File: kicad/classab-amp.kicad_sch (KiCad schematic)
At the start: 65 parts, among them J1 SPEAKER, J3 INPUT, Q1 BC547, Q10 MJL3218C, Q11 BD140, Q12 MJL1302C, Q13 BC547, Q14 BC557, Q2 BC547, Q3 BC557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

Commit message: Adjustments
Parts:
- removed D10, D7, D8, D9: 1N5400, Diode_THT:D_DO-201AD_P15.24mm_Horizontal, symbol Diode:1N5400
- removed D3, D6: 1N4001, Diode_THT:D_DO-41_SOD81_P10.16mm_Horizontal, symbol Diode:1N4001
- added D10, D3, D6, D7, D8, D9: 1N4004, Diode_THT:D_DO-41_SOD81_P10.16mm_Horizontal, symbol Diode:1N4004
- C4: footprint Capacitor_THT:CP_Radial_D4.0mm_P1.50mm -> Capacitor_THT:CP_Radial_D8.0mm_P5.00mm
- C6: footprint (none) -> Capacitor_THT:C_Rect_L7.2mm_W3.0mm_P5.00mm_FKS2_FKP2_MKS2_MKP2
- R13, R6: value 47k -> 10k
- R5: value 2.2k -> 1k
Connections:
- net B+: now also D7.1 (K), D8.1 (K)
- net B-: now also D10.2 (A), D9.2 (A)
- net GND: now also D10.1 (K), D7.2 (A)
- net at Q10.3 (E), R16.1, R18.2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: now also D8.2 (A)
- net at C5.2, C6.1, Q6.2 (C)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: now also D6.2 (A)
- net at C12.1, Q14.1 (C): now also D3.2 (A)
- net at Q12.3 (E), R17.2, R19.1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: now also D9.1 (K)
- net at C11.1, Q13.1 (C): now also D6.1 (K)
- net at C6.2, Q11.3 (B), Q7.1 (E)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: now also D3.1 (K)
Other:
- moved on the sheet: R6

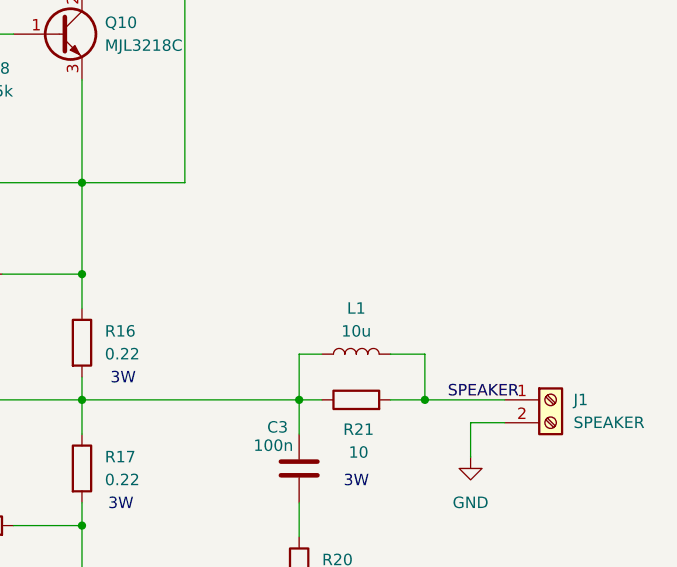
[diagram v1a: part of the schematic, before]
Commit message: Added Zobel image
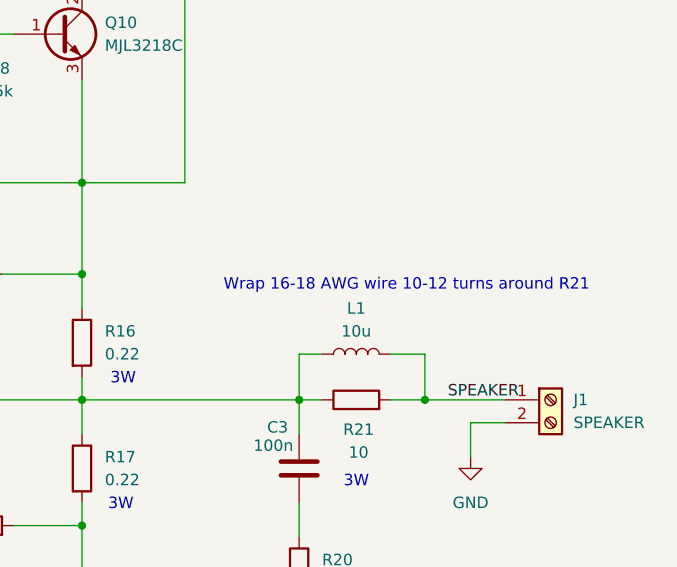
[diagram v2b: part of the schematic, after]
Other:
- note added: "Wrap 16-18 AWG wire 10-12 turns around R21"
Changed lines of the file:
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@@
+		)
+	)
+	(text "Wrap 16-18 AWG wire 10-12 turns around R21"
+		(exclude_from_sim no)
+		(at 257.048 74.93 0)
+		(effects
+			(font
+				(size 1.27 1.27)
+			)
 		)
 	)

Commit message: Added ver 2 SPICE design
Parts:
- added C7: 10n, Capacitor_THT:C_Rect_L7.2mm_W3.0mm_P5.00mm_FKS2_FKP2_MKS2_MKP2, symbol Device:C
- R15: value 10 -> 220
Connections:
- net CHASSIS: now also C7.2
- net GND: now also C7.1
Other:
- moved on the sheet: D8, R15
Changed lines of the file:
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@@
 	)
 	(junction
-		(at 64.77 115.57)
+		(at 53.34 118.11)
 		(diameter 0)
 		(color 0 0 0 0)
@@
 	(wire
 		(pts
+			(xy 64.77 102.87) (xy 64.77 106.68)
+		)
+		(stroke
+			(width 0)
+			(type default)
+		)
+	)
+	(wire
+		(pts
 			(xy 168.91 107.95) (xy 168.91 118.11)
 		)
@@
 	(wire
 		(pts
-			(xy 232.41 29.21) (xy 232.41 34.29)
+			(xy 232.41 29.21) (xy 232.41 35.56)
 		)
 		(stroke
@@
 	(wire
 		(pts
-			(xy 64.77 115.57) (xy 64.77 116.84)
+			(xy 53.34 118.11) (xy 53.34 119.38)
 		)
 		(stroke
@@
 	(wire
 		(pts
-			(xy 182.88 134.62) (xy 189.23 134.62)
+			(xy 180.34 134.62) (xy 189.23 134.62)
 		)
 		(stroke
@@
 	(wire
 		(pts
-			(xy 176.53 118.11) (xy 182.88 118.11)
+			(xy 176.53 118.11) (xy 180.34 118.11)
 		)
 		(stroke
@@
 	(wire
 		(pts
-			(xy 182.88 118.11) (xy 182.88 134.62)
+			(xy 180.34 118.11) (xy 180.34 134.62)
 		)
 		(stroke
@@
 	(wire
 		(pts
-			(xy 64.77 114.3) (xy 64.77 115.57)
+			(xy 53.34 114.3) (xy 53.34 118.11)
 		)
 		(stroke
@@
 	(wire
 		(pts
+			(xy 53.34 118.11) (xy 64.77 118.11)
+		)
+		(stroke
+			(width 0)
+			(type default)
+		)
+	)
+	(wire
+		(pts
 			(xy 180.34 68.58) (xy 180.34 38.1)
 		)
@@
 	(wire
 		(pts
+			(xy 53.34 102.87) (xy 64.77 102.87)
+		)
+		(stroke
+			(width 0)
+			(type default)
+		)
+	)
+	(wire
+		(pts
 			(xy 168.91 128.27) (xy 168.91 130.81)
 		)
@@
 	(wire
 		(pts
+			(xy 64.77 114.3) (xy 64.77 118.11)
+		)
+		(stroke
+			(width 0)
+			(type default)
+		)
+	)
+	(wire
+		(pts
 			(xy 46.99 95.25) (xy 46.99 96.52)
 		)
@@
 	(wire
 		(pts
-			(xy 64.77 106.68) (xy 64.77 102.87)
+			(xy 53.34 106.68) (xy 53.34 102.87)
 		)
 		(stroke
@@
 	(wire
 		(pts
-			(xy 232.41 41.91) (xy 232.41 63.5)
+			(xy 232.41 43.18) (xy 232.41 63.5)
 		)
 		(stroke
@@
 	(text "3W"
 		(exclude_from_sim no)
-		(at 68.072 115.57 0)
+		(at 56.896 114.3 0)
 		(effects
 			(font
@@
 	(symbol
 		(lib_id "Diode:1N4004")
-		(at 232.41 38.1 270)
+		(at 232.41 39.37 270)
 		(unit 1)
 		(exclude_from_sim no)
@@
 		(fields_autoplaced yes)
 		(property "Reference" "D8"
-			(at 234.95 36.8299 90)
+			(at 234.95 38.0999 90)
 			(effects
 				(font
@@
 		)
 		(property "Value" "1N4004"
-			(at 234.95 39.3699 90)
+			(at 234.95 40.6399 90)
 			(effects
 				(font
@@
 		)
 		(property "Footprint" "Diode_THT:D_DO-41_SOD81_P10.16mm_Horizontal"
-			(at 227.965 38.1 0)
+			(at 227.965 39.37 0)
 			(effects
 				(font
@@
 		)
 		(property "Datasheet" "http://www.vishay.com/docs/88503/1n4001.pdf"
-			(at 232.41 38.1 0)
+			(at 232.41 39.37 0)
 			(effects
 				(font
@@
 		)
 		(property "Description" "400V 1A General Purpose Rectifier Diode, DO-41"
-			(at 232.41 38.1 0)
+			(at 232.41 39.37 0)
 			(effects
 				(font
@@
 		)
 		(property "Sim.Device" "D"
-			(at 232.41 38.1 0)
+			(at 232.41 39.37 0)
 			(effects
 				(font
@@
 		)
 		(property "Sim.Pins" "1=K 2=A"
-			(at 232.41 38.1 0)
+			(at 232.41 39.37 0)
 			(effects
 				(font
@@
 	(symbol
 		(lib_id "Device:R")
-		(at 64.77 110.49 180)
+		(at 53.34 110.49 180)
 		(unit 1)
 		(exclude_from_sim no)
@@
 		(fields_autoplaced yes)
 		(property "Reference" "R15"
-			(at 67.31 109.2199 0)
+			(at 55.88 109.2199 0)
 			(effects
 				(font
@@
 			)
 		)
-		(property "Value" "10"
-			(at 67.31 111.7599 0)
+		(property "Value" "220"
+			(at 55.88 111.7599 0)
 			(effects
 				(font
@@
 		)
 		(property "Footprint" "Resistor_THT:R_Axial_DIN0414_L11.9mm_D4.5mm_P15.24mm_Horizontal"
-			(at 66.548 110.49 90)
+			(at 55.118 110.49 90)
 			(effects
 				(font
@@
 		)
 		(property "Datasheet" "~"
-			(at 64.77 110.49 0)
+			(at 53.34 110.49 0)
 			(effects
 				(font
@@
 		)
 		(property "Description" "Resistor"
-			(at 64.77 110.49 0)
+			(at 53.34 110.49 0)
 			(effects
 				(font
@@
 	(symbol
 		(lib_id "power:PWR_FLAG")
-		(at 64.77 115.57 90)
+		(at 53.34 118.11 90)
 		(unit 1)
 		(exclude_from_sim no)
@@
 		(fields_autoplaced yes)
 		(property "Reference" "#FLG01"
-			(at 62.865 115.57 0)
+			(at 51.435 118.11 0)
 			(effects
 				(font
@@
 		)
 		(property "Value" "PWR_FLAG"
-			(at 60.96 115.5699 90)
+			(at 49.53 118.1099 90)
 			(effects
 				(font
@@
 		)
 		(property "Footprint" ""
-			(at 64.77 115.57 0)
+			(at 53.34 118.11 0)
 			(effects
 				(font
@@
 		)
 		(property "Datasheet" "~"
-			(at 64.77 115.57 0)
+			(at 53.34 118.11 0)
 			(effects
 				(font
@@
 		)
 		(property "Description" "Special symbol for telling ERC where power comes from"
-			(at 64.77 115.57 0)
+			(at 53.34 118.11 0)
 			(effects
 				(font
@@
 	(symbol
 		(lib_id "power:GNDPWR")
-		(at 64.77 116.84 0)
+		(at 53.34 119.38 0)
 		(unit 1)
 		(exclude_from_sim no)
@@
 		(fields_autoplaced yes)
 		(property "Reference" "#PWR011"
-			(at 64.77 121.92 0)
+			(at 53.34 124.46 0)
 			(effects
 				(font
@@
 		)
 		(property "Value" "CHASSIS"
-			(at 64.643 120.65 0)
+			(at 53.213 123.19 0)
 			(effects
 				(font
@@
 		)
 		(property "Footprint" ""
-			(at 64.77 118.11 0)
+			(at 53.34 120.65 0)
 			(effects
 				(font
@@
 		)
 		(property "Datasheet" ""
-			(at 64.77 118.11 0)
+			(at 53.34 120.65 0)
 			(effects
 				(font
@@
 		)
 		(property "Description" "Power symbol creates a global label with name \"GNDPWR\" , global ground"
-			(at 64.77 116.84 0)
+			(at 53.34 119.38 0)
 			(effects
 				(font
@@
 					(unit 1)
 				)
+			)
+		)
+	)
+	(symbol
+		(lib_id "Device:C")
+		(at 64.77 110.49 0)
+		(unit 1)
+		(exclude_from_sim no)
+		(in_bom yes)
+		(on_board yes)
+		(dnp no)
+		(fields_autoplaced yes)
+		(property "Reference" "C7"
+			(at 68.58 109.2199 0)
+			(effects
+				(font
+					(size 1.27 1.27)
+				)
+				(justify left)
+			)
+		)
+		(property "Value" "10n"
+			(at 68.58 111.7599 0)
+			(effects
+				(font
+					(size 1.27 1.27)
+				)
+				(justify left)
+			)
+		)
+		(property "Footprint" "Capacitor_THT:C_Rect_L7.2mm_W3.0mm_P5.00mm_FKS2_FKP2_MKS2_MKP2"
+			(at 65.7352 114.3 0)
+			(effects
+				(font
+					(size 1.27 1.27)
+				)
+				(hide yes)
+			)
+		)
+		(property "Datasheet" "~"
+			(at 64.77 110.49 0)
+			(effects
+				(font
+					(size 1.27 1.27)
+				)
+				(hide yes)
+			)
+		)
+		(property "Description" "Unpolarized capacitor"
+			(at 64.77 110.49 0)
+			(effects
+				(font
+					(size 1.27 1.27)
+				)
+				(hide yes)
+			)
+		)
+		(pin "2"
+		)
+		(pin "1"
+		)
+		(instances
+			(project ""
+				(path "/856f1e14-388c-4d87-abe9-3c0c6310ec29"
+					(reference "C7")
+					(unit 1)
+				)

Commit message: Update gerber files
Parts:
- added C8: 4.7n, Capacitor_THT:C_Rect_L7.2mm_W3.0mm_P5.00mm_FKS2_FKP2_MKS2_MKP2, symbol Device:C
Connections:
- net at C6.2, D3.1 (K), Q11.3 (B)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: now also C8.1
- net at D4.2 (A), Q8.3 (B), R13.1: now also C8.2
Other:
- moved on the sheet: C13, C15, D10, D4, D5, Q8, R13, R14

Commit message: WIP
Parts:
- removed R8: 1k, Resistor_THT:R_Axial_DIN0204_L3.6mm_D1.6mm_P7.62mm_Horizontal, symbol Device:R
- added R22, R23: 150, Resistor_THT:R_Axial_DIN0204_L3.6mm_D1.6mm_P7.62mm_Horizontal, symbol Device:R
- Q10: value MJL3218C -> MJL3281C
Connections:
- net at C5.1, Q6.3 (B): now also Q1.1 (C), Q3.1 (C)
- new net: Q5.1 (C), R22.1, R23.1
- new net: Q2.3 (E), R23.2
- new net: Q1.3 (E), R22.2
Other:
- note added: "C8 optional. Omit if amp is stable without it."
- note added: "R22 and R23 should be closely matched."
- moved on the sheet: C6
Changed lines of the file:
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@@
 	)
 	(junction
-		(at 176.53 118.11)
-		(diameter 0)
-		(color 0 0 0 0)
-	)
-	(junction
 		(at 115.57 29.21)
 		(diameter 0)
@@
 	)
 	(junction
+		(at 179.07 118.11)
+		(diameter 0)
+		(color 0 0 0 0)
+	)
+	(junction
 		(at 64.77 102.87)
 		(diameter 0)
@@
 	(wire
 		(pts
+			(xy 114.3 99.06) (xy 115.57 99.06)
+		)
+		(stroke
+			(width 0)
+			(type default)
+		)
+	)
+	(wire
+		(pts
 			(xy 255.27 82.55) (xy 259.08 82.55)
 		)
@@
 	(wire
 		(pts
-			(xy 134.62 68.58) (xy 154.94 68.58)
-		)
-		(stroke
-			(width 0)
-			(type default)
-		)
-	)
-	(wire
-		(pts
 			(xy 154.94 100.33) (xy 154.94 102.87)
 		)
@@
 	(wire
 		(pts
-			(xy 180.34 134.62) (xy 189.23 134.62)
+			(xy 179.07 134.62) (xy 189.23 134.62)
 		)
 		(stroke
@@
 	(wire
 		(pts
-			(xy 176.53 115.57) (xy 176.53 118.11)
+			(xy 179.07 106.68) (xy 179.07 118.11)
 		)
 		(stroke
@@
 	(wire
 		(pts
-			(xy 176.53 118.11) (xy 180.34 118.11)
-		)
-		(stroke
-			(width 0)
-			(type default)
-		)
-	)
-	(wire
-		(pts
 			(xy 154.94 118.11) (xy 168.91 118.11)
 		)
@@
 	(wire
 		(pts
-			(xy 168.91 118.11) (xy 176.53 118.11)
+			(xy 168.91 118.11) (xy 179.07 118.11)
 		)
 		(stroke
@@
 	(wire
 		(pts
-			(xy 180.34 118.11) (xy 180.34 134.62)
+			(xy 179.07 118.11) (xy 179.07 134.62)
 		)
 		(stroke
@@
 	(wire
 		(pts
+			(xy 104.14 99.06) (xy 105.41 99.06)
+		)
+		(stroke
+			(width 0)
+			(type default)
+		)
+	)
+	(wire
+		(pts
 			(xy 220.98 111.76) (xy 220.98 120.65)
 		)
@@
 	(wire
 		(pts
-			(xy 176.53 107.95) (xy 176.53 90.17)
+			(xy 179.07 99.06) (xy 179.07 90.17)
 		)
 		(stroke
@@
 	(wire
 		(pts
-			(xy 105.41 99.06) (xy 115.57 99.06)
+			(xy 105.41 99.06) (xy 106.68 99.06)
 		)
 		(stroke
@@
 	(wire
 		(pts
-			(xy 95.25 68.58) (xy 127 68.58)
+			(xy 95.25 68.58) (xy 154.94 68.58)
 		)
 		(stroke
@@
 	(wire
 		(pts
-			(xy 168.91 90.17) (xy 176.53 90.17)
+			(xy 168.91 90.17) (xy 179.07 90.17)
 		)
 		(stroke
@@
 	(wire
 		(pts
-			(xy 95.25 99.06) (xy 105.41 99.06)
+			(xy 95.25 99.06) (xy 96.52 99.06)
 		)
 		(stroke
@@
 		)
 	)
+	(text "R22 and R23 should be\nclosely matched."
+		(exclude_from_sim no)
+		(at 117.348 104.14 0)
+		(effects
+			(font
+				(size 1.27 1.27)
+			)
+		)
+	)
 	(text "3W"
 		(exclude_from_sim no)
@@
 		)
 	)
+	(text "C8 optional. Omit if amp \nis stable without it."
+		(exclude_from_sim no)
+		(at 139.954 122.936 0)
+		(effects
+			(font
+				(size 1.27 1.27)
+			)
+		)
+	)
 	(label "LTP COM"
 		(at 115.57 76.2 0)
@@
 	)
 	(symbol
+		(lib_id "Device:R")
+		(at 110.49 99.06 90)
+		(unit 1)
+		(exclude_from_sim no)
+		(in_bom yes)
+		(on_board yes)
+		(dnp no)
+		(fields_autoplaced yes)
+		(property "Reference" "R23"
+			(at 110.49 92.71 90)
+			(effects
+				(font
+					(size 1.27 1.27)
+				)
+			)
+		)
+		(property "Value" "150"
+			(at 110.49 95.25 90)
+			(effects
+				(font
+					(size 1.27 1.27)
+				)
+			)
+		)
+		(property "Footprint" "Resistor_THT:R_Axial_DIN0204_L3.6mm_D1.6mm_P7.62mm_Horizontal"
+			(at 110.49 100.838 90)
+			(effects
+				(font
+					(size 1.27 1.27)
+				)
+				(hide yes)
+			)
+		)
+		(property "Datasheet" "~"
+			(at 110.49 99.06 0)
+			(effects
+				(font
+					(size 1.27 1.27)
+				)
+				(hide yes)
+			)
+		)
+		(property "Description" "Resistor"
+			(at 110.49 99.06 0)
+			(effects
+				(font
+					(size 1.27 1.27)
+				)
+				(hide yes)
+			)
+		)
+		(pin "1"
+		)
+		(pin "2"
+		)
+		(instances
+			(project ""
+				(path "/856f1e14-388c-4d87-abe9-3c0c6310ec29"
+					(reference "R23")
+					(unit 1)
+				)
+			)
+		)
+	)
+	(symbol
 		(lib_id "Device:C_Polarized")
 		(at 220.98 152.4 180)
@@
 	)
 	(symbol
-		(lib_id "Device:R")
-		(at 130.81 68.58 270)
-		(unit 1)
-		(exclude_from_sim no)
-		(in_bom yes)
-		(on_board yes)
-		(dnp no)
-		(fields_autoplaced yes)
-		(property "Reference" "R8"
-			(at 130.81 62.23 90)
-			(effects
-				(font
-					(size 1.27 1.27)
-				)
-			)
-		)
-		(property "Value" "1k"
-			(at 130.81 64.77 90)
-			(effects
-				(font
-					(size 1.27 1.27)
-				)
-			)
-		)
-		(property "Footprint" "Resistor_THT:R_Axial_DIN0204_L3.6mm_D1.6mm_P7.62mm_Horizontal"
-			(at 130.81 66.802 90)
-			(effects
-				(font
-					(size 1.27 1.27)
-				)
-				(hide yes)
-			)
-		)
-		(property "Datasheet" "~"
-			(at 130.81 68.58 0)
-			(effects
-				(font
-					(size 1.27 1.27)
-				)
-				(hide yes)
-			)
-		)
-		(property "Description" "Resistor"
-			(at 130.81 68.58 0)
-			(effects
-				(font
-					(size 1.27 1.27)
-				)
-				(hide yes)
-			)
-		)
-		(pin "2"
-		)
-		(pin "1"
-		)
-		(instances
-			(project ""
-				(path "/856f1e14-388c-4d87-abe9-3c0c6310ec29"
-					(reference "R8")
-					(unit 1)
-				)
-			)
-		)
-	)
-	(symbol
 		(lib_id "Transistor_BJT:BD139")
 		(at 204.47 38.1 0)
@@
 	(symbol
 		(lib_id "Device:C")
-		(at 176.53 111.76 0)
+		(at 179.07 102.87 0)
 		(unit 1)
 		(exclude_from_sim no)
@@
 		(on_board yes)
 		(dnp no)
-		(fields_autoplaced yes)
 		(property "Reference" "C6"
-			(at 180.34 110.4899 0)
+			(at 181.61 101.6 0)
 			(effects
 				(font
@@
 		)
 		(property "Value" "100n"
-			(at 180.34 113.0299 0)
+			(at 181.61 104.14 0)
 			(effects
 				(font
@@
 		)
 		(property "Footprint" "Capacitor_THT:C_Rect_L7.2mm_W3.0mm_P5.00mm_FKS2_FKP2_MKS2_MKP2"
-			(at 177.4952 115.57 0)
+			(at 180.0352 106.68 0)
 			(effects
 				(font
@@
 		)
 		(property "Datasheet" "~"
-			(at 176.53 111.76 0)
+			(at 179.07 102.87 0)
 			(effects
 				(font
@@
 		)
 		(property "Description" "Unpolarized capacitor"
-			(at 176.53 111.76 0)
+			(at 179.07 102.87 0)
 			(effects
 				(font
@@
 			)
 		)
-		(property "Value" "MJL3218C"
+		(property "Value" "MJL3281C"
 			(at 223.52 48.2599 0)
 			(effects
@@
 	)
 	(symbol
+		(lib_id "Device:R")
+		(at 100.33 99.06 270)
+		(unit 1)
+		(exclude_from_sim no)
+		(in_bom yes)
+		(on_board yes)
+		(dnp no)
+		(fields_autoplaced yes)
+		(property "Reference" "R22"
+			(at 100.33 92.71 90)
+			(effects
+				(font
+					(size 1.27 1.27)
+				)
+			)
+		)
+		(property "Value" "150"
+			(at 100.33 95.25 90)
+			(effects
+				(font
+					(size 1.27 1.27)
+				)
+			)
+		)
+		(property "Footprint" "Resistor_THT:R_Axial_DIN0204_L3.6mm_D1.6mm_P7.62mm_Horizontal"
+			(at 100.33 97.282 90)
+			(effects
+				(font
+					(size 1.27 1.27)
+				)
+				(hide yes)
+			)
+		)
+		(property "Datasheet" "~"
+			(at 100.33 99.06 0)
+			(effects
+				(font
+					(size 1.27 1.27)
+				)
+				(hide yes)
+			)
+		)
+		(property "Description" "Resistor"
+			(at 100.33 99.06 0)
+			(effects
+				(font
+					(size 1.27 1.27)
+				)
+				(hide yes)
+			)
+		)
+		(pin "1"
+		)
+		(pin "2"
+		)
+		(instances
+			(project ""
+				(path "/856f1e14-388c-4d87-abe9-3c0c6310ec29"
+					(reference "R22")
+					(unit 1)
+				)
+			)
+		)
+	)
+	(symbol
 		(lib_id "Transistor_BJT:BC547")
 		(at 191.77 73.66 0)
@@
 		(on_board yes)
 		(dnp no)
-		(fields_autoplaced yes)
 		(property "Reference" "Q7"
-			(at 171.45 101.5999 0)
+			(at 171.196 104.902 0)
 			(effects
 				(font
@@
 		)
 		(property "Value" "BD139"
-			(at 171.45 104.1399 0)
+			(at 170.18 107.696 0)
 			(effects
 				(font
